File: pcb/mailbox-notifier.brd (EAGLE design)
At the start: 35 x 100 mm, 24 parts, among them Q1 AO3401, U1 MIC23155, U2 LTC2943-X, U3 FS312F-G, U4 FS8205, U5 MCP73832, U6 EFM32PG1B200_Q32, U7 RFM69HW

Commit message: PCB Work
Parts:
- removed U4: FS8205, Fortune:SOT23-6
- added C4: 100uF, Capacitor:CAP1206
- added C49: 100nF, Capacitor:CAP0603
- added CON1: 3P-SH-SIDE, JST:SH-03-SIDE
- added D2: SMAJ5.0A, TVS:DO214AC
- added F1: 1A Hold, PTC Fuses:1206
- added R1, R2: 5.1K Ohms, Resistor:RES0603
- added R58: 1K Ohms, Resistor:RES0603
- added R59: 100 Ohms, Resistor:RES0603
- added R63: 10M Ohm, Resistor:RES0603
- added U14: FS312F-G, Fortune:SOT23-6
- added U16: FS8205, Fortune:SOT23-6
- added U8: SI7021, Silicon Labs:DFN6
- U3: value FS312F-G -> 74LVC1G17; device Fortune:SOT23-6 -> Logic:SC70-5
- moved U6 81.8 mm to (18.0, 52.3)
- moved U3 79.6 mm to (-47.6, 32.8)
- moved TC1 14.7 mm to (3.50, 51.4)
- moved USB1 0.40 mm to (17.5, 98.6)
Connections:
- removed net +: BAT1.+
- removed net -: BAT1.-
- new net 5V0: C4.1, D1.A, D2.C, F1.1, Q1.1
- new net EXT_TRIG: U3.4
- new net GBAT: BAT1.-, C49.2, R63.2, U14.6, U16.3
- new net N$2: BAT1.+, U2.8
- new net N$3: R1.2, USB1.CC2
- new net N$4: F1.2, USB1.VBUS@0, USB1.VBUS@1
- new net N$47: U14.3, U16.6
- new net N$48: U14.1, U16.4
- new net N$49: R59.1, U14.5
- new net N$5: R2.2, USB1.CC1
- new net N$50: R58.1, U14.2
- new net N$6: CON1.2, U3.2
- new net VBAT: C49.1, Q1.3, R59.2, U2.1
- new net VIN: D1.C, Q1.2
- net 2V8: now also CON1.1, U3.5
- net GND: now also C4.2, CON1.3, D2.A, R1.1, R2.1, R58.2, R63.1, U16.1, U3.3, USB1.GND@0, USB1.GND@1, USB1.SHIELD@0, USB1.SHIELD@1, USB1.SHIELD@2, USB1.SHIELD@3

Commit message: PCB work
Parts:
- removed C49: 100nF, Capacitor:CAP0603
- removed R58: 1K Ohms, Resistor:RES0603
- removed R59: 100 Ohms, Resistor:RES0603
- removed R63: 10M Ohm, Resistor:RES0603
- removed U14: FS312F-G, Fortune:SOT23-6
- removed U16: FS8205, Fortune:SOT23-6
- removed U2: LTC2943-X, Analog Devices:DFN8
- removed U3: 74LVC1G17, Logic:SC70-5
- added C10: 2.2uF, Capacitor:CAP0603
- added C11: 100uF, Capacitor:CAP1206
- added C12, C14, C15, C20, C21, C23, C7: 100nF, Capacitor:CAP0603
- added C17, C24: 1uF, Capacitor:CAP0603
- added C22, C9: 470pF, Capacitor:CAP0603
- added C5, C6: 10uF, Capacitor:CAP0603
- added C8: 4.7uF, Capacitor:CAP0603
- added D3: SK9822, LED:2020
- added L2: 4.7uH, Inductor:IND0603
- added R10: 324K Ohms, Resistor:RES0603
- added R11: 91K Ohms, Resistor:RES0603
- added R12: 10M Ohm, Resistor:RES0603
- added R15: 10K Ohms, Resistor:RES0603
- added R16, R17, R18, R19, R20, R9: 100K Ohms, Resistor:RES0603
- added R21: 2K Ohms, Resistor:RES0603
- added R3: 5.1K Ohms, Resistor:RES0603
- added R7: 1K Ohms, Resistor:RES0603
- added R8: 100 Ohms, Resistor:RES0603
- added U10: SI7021, Silicon Labs:DFN6
- added U11: 74LVC1G17, Logic:SC70-5
- added U12: MIC2019, Microchip:SOT23-6
- added U4: MIC23155, Microchip:DFN10
- added U9: RFM69HW, HopeRF:RFM69W-XXXS2
- added X1: 40MHz, Crystal:4-SMD-3225
- C16: value 100nF -> 4.7uF
- C18: value 1uF -> 100nF
- C19: value 4.7uF -> 100nF
- C2: value 100nF -> 100uF; device Capacitor:CAP0603 -> Capacitor:CAP1206
- D1: value B0530W -> SMAJ5.0A; device Generic Diode:SOD-123 -> TVS:DO214AC
- D2: value SMAJ5.0A -> B0530W; device TVS:DO214AC -> Generic Diode:SOD-123
- L1: value 4.7uH -> 2.2uH; device Inductor:IND0603 -> Inductor:IND0805
- R13, R4: value 10K Ohms -> 100K Ohms
- R2: value 5.1K Ohms -> 2.2K Ohms
- U1: value MIC23155 -> MCP73832; device Microchip:DFN10 -> Microchip:SOT23-5
- U5: value MCP73832 -> FS312F-G; device Microchip:SOT23-5 -> Fortune:SOT23-6
- U6: value EFM32PG1B200_Q32 -> FS8205; device EFM32:QFN32 -> Fortune:SOT23-6
- U7: value RFM69HW -> EFM32PG1B200_Q32; device HopeRF:RFM69W-XXXS2 -> EFM32:QFN32
- U8: value SI7021 -> SST26VF016B; device Silicon Labs:DFN6 -> Microchip:WSOIC8
- moved RFCON1 105.3 mm to (3.00, 17.0)
- moved U5 93.9 mm to (28.9, 86.7)
- moved R14 90.1 mm to (28.2, 43.2), turned to 90 degrees
- moved S1 90.1 mm to (4.20, 39.6), turned to 90 degrees
- moved U8 84.8 mm to (17.7, 24.7), turned to 90 degrees
- moved CON1 81.6 mm to (33.0, 64.4), turned to 90 degrees
- moved U1 80.4 mm to (29.0, 83.2)
- moved F1 77.5 mm to (17.7, 88.5), turned to 90 degrees
- moved C4 76.9 mm to (29.2, 72.5)
- moved L1 72.3 mm to (-92.4, 76.1)
- moved R4 71.5 mm to (-77.3, 36.5)
- moved R1 68.9 mm to (10.0, 96.5)
- moved D2 67.7 mm to (-20.3, 120.7)
- moved C2 63.6 mm to (14.3, 88.5), turned to 90 degrees
- moved C18 60.9 mm to (-61.2, 54.8)
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- renumbered C1 to C13
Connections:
- removed net N$2: BAT1.+, U2.8
- new net !FLASH_CS: R16.1, U8.1
- new net 2V8_PGOOD: R9.1, U4.5
- new net BAT_STAT: R4.1, U1.1
- new net I2C0_SCL: R15.1, U10.6
- new net I2C0_SDA: R14.1, U10.1
- new net LED_EN: U12.3
- new net N$10: R2.2, U1.5
- new net N$11: R21.2, U12.5
- new net N$12: L1.1, U4.1
- new net N$13: R10.1, R11.2, U4.4
- new net N$14: C9.1, U4.6
- new net N$15: C24.1, D3.5, U12.6
- new net N$16: U7.6, X1.1
- new net N$17: U7.7, X1.3
- new net US1_CLK: D3.4
- new net US1_MOSI: D3.3
- new net VBAT_SENSE: C22.1, R19.1, R20.2
- new net VIN1: C3.1
- net !RFM_CS: now also R18.1, U7.13, U9.15; no longer R14.1, U6.13, U7.15
- net !RST: now also R13.1, U7.8; no longer R4.1, U6.8
- net 1V8: now also C16.1, L2.1, U7.28; no longer C19.1, L1.1, U6.28
- net 2V8: now also C10.1, C11.1, C14.1, C15.1, C18.1, C19.2, C20.1, C21.1, C23.1, L1.2, R10.2, R13.2, R15.2, R16.2, R18.2, R9.2, U10.5, U11.5, U12.1, U4.3, U7.22, U7.27, U7.30, U7.5, U8.3, U8.7, U8.8, U9.8; no longer C16.2, C2.1, C3.1, U3.5, U6.22, U6.27, U6.30, U6.5, U7.8
- net 5V0: now also C2.1, D1.C, D2.A, U1.4; no longer C4.1, D1.A, D2.C
- net EXT_TRIG: now also U11.4; no longer U3.4
- net GBAT: now also C12.2, R12.2, U5.6, U6.3; no longer C49.2, R63.2, U14.6, U16.3
- net GND: now also C10.2, C11.2, C14.2, C15.2, C16.2, C17.1, C18.2, C19.1, C20.2, C21.2, C22.2, C23.2, C24.2, C5.2, C6.2, C7.2, C8.2, C9.2, D1.A, D3.2, R11.1, R12.1, R17.1, R20.1, R21.1, R3.1, R7.1, U1.2, U10.2, U11.3, U12.2, U4.10, U4.11, U4.7, U6.1, U7.25, U7.33, U8.4, U9.11, U9.9, X1.2, X1.4; no longer C16.1, C18.1, C19.2, D2.A, R13.1, R58.2, R63.1, U16.1, U3.3, U6.25, U6.33, U7.11, U7.9
- net N$1: now also U9.10; no longer U7.10
- net N$19: now also L2.2, U7.26; no longer L1.2, U6.26
- net N$20: now also C17.2, U7.29; no longer C18.2, U6.29
- net N$47: now also U5.3, U6.6; no longer U14.3, U16.6
- net N$48: now also U5.1, U6.4; no longer U14.1, U16.4
- net N$49: now also R8.1, U5.5; no longer R59.1, U14.5
- net N$5: now also R3.2; no longer R2.2
- net N$50: now also R7.2, U5.2; no longer R58.1, U14.2
- net N$6: now also U11.2; no longer U3.2
- net RFM_IRQ: now also U7.31, U9.2; no longer U6.31, U7.2
- net RFM_RST: now also R17.2, U7.12, U9.1; no longer R13.2, U6.12, U7.1
- net SWCLK: now also U7.1; no longer U6.1
- net SWDIO: now also U7.2; no longer U6.2
- net SWO: now also U7.3; no longer U6.3
- net US0_CLK: now also U7.14, U8.6, U9.12; no longer U6.14, U7.12
- net US0_MISO: now also U7.16, U8.2, U9.13; no longer U6.16, U7.13
- net US0_MOSI: now also U7.15, U8.5, U9.14; no longer U6.15, U7.14
- net VBAT: now also BAT1.+, C12.1, C4.1, R19.2, R8.2, U1.3; no longer C49.1, R59.2, U2.1
- net VIN: now also C5.1, C6.1, C7.1, C8.1, D2.C, U4.2, U4.8, U4.9; no longer D1.C
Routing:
- net N$4: track 0.00 -> 9.10 mm
- net N$3: track 0.00 -> 7.66 mm
- net N$5: track 0.00 -> 7.16 mm
- net 5V0: track 0.00 -> 7.09 mm
- net N$1: track 0.00 -> 3.62 mm
- added copper zone on layer 1, net GND
- added copper zone on layer 16, net GND

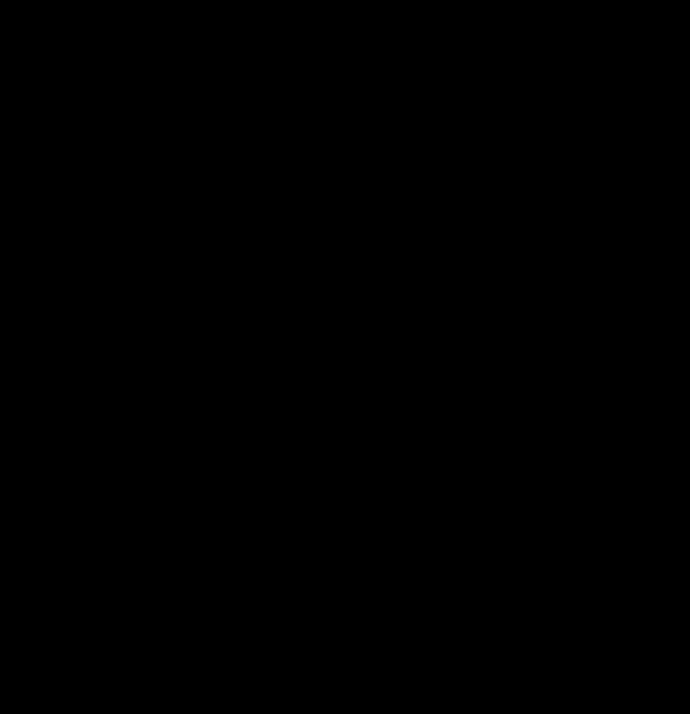
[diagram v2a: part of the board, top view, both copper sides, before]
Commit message: Add power switch to external trigger
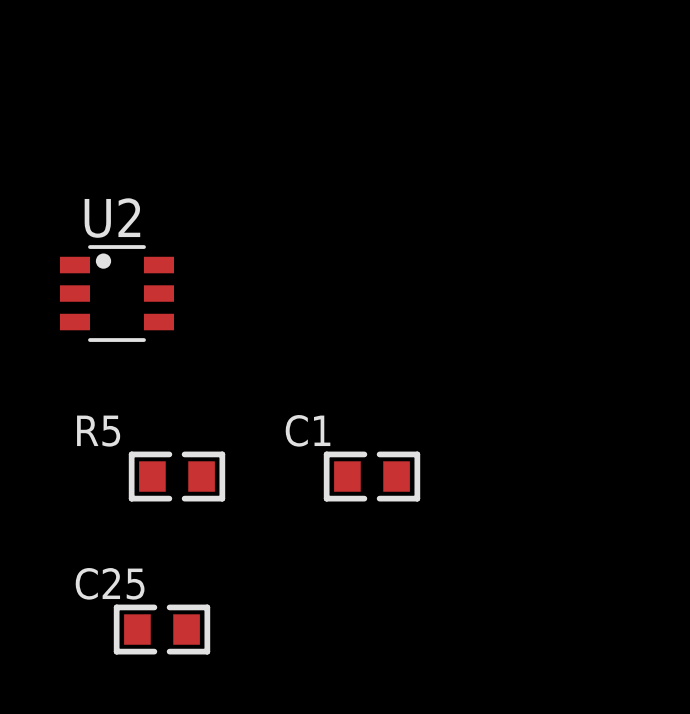
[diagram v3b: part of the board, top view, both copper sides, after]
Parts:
- added C1: 100nF, Capacitor:CAP0603
- added C25: 1uF, Capacitor:CAP0603
- added R5: 2K Ohms, Resistor:RES0603
- added U2: MIC2019, Microchip:SOT23-6
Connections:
- new net EXT_EN: U2.3
- new net N$2: R5.2, U2.5
- new net N$7: C25.1, CON1.1, U2.6
- net 2V8: now also C1.1, U2.1; no longer CON1.1
- net GND: now also C1.2, C25.2, R5.1, U2.2
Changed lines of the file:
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@@
 <?xml version="1.0" encoding="utf-8"?>
 <!DOCTYPE eagle SYSTEM "eagle.dtd">
-<eagle version="9.3.0">
+<eagle version="9.3.2">
 <drawing>
 <settings>
@@
 <attribute name="NAME" x="8.86" y="51.54" size="0.762" layer="25" font="vector" ratio="10"/>
 </element>
+<element name="U2" library="Microchip" package="SOT23-6" value="MIC2019" x="-94.5" y="-8.9" smashed="yes">
+<attribute name="NAME" x="-95.714" y="-7.0175" size="1.27" layer="25" ratio="10"/>
+<attribute name="VALUE" x="-95.714" y="-11.989" size="1.27" layer="27" ratio="10"/>
+</element>
+<element name="C1" library="Capacitor" package="CAP0603" value="100nF" x="-86" y="-15" smashed="yes">
+<attribute name="NAME" x="-88.9464" y="-13.984" size="1.016" layer="25" ratio="10" rot="SR0"/>
+<attribute name="VALUE" x="-88.9464" y="-17.032" size="1.016" layer="27" ratio="10" rot="SR0"/>
+</element>
+<element name="R5" library="Resistor" package="RES0603" value="2K Ohms" x="-92.5" y="-15" smashed="yes">
+<attribute name="NAME" x="-95.9544" y="-13.984" size="1.016" layer="25" ratio="10" rot="SR0"/>
+<attribute name="VALUE" x="-95.9544" y="-17.032" size="1.016" layer="27" ratio="10" rot="SR0"/>
+</element>
+<element name="C25" library="Capacitor" package="CAP0603" value="1uF" x="-93" y="-20.1" smashed="yes">
+<attribute name="NAME" x="-95.9464" y="-19.084" size="1.016" layer="25" ratio="10" rot="SR0"/>
+<attribute name="VALUE" x="-95.9464" y="-22.132" size="1.016" layer="27" ratio="10" rot="SR0"/>
+</element>
 </elements>
 <signals>
@@
 <contactref element="U9" pad="8"/>
 <contactref element="R18" pad="2"/>
-<contactref element="CON1" pad="1"/>
 <contactref element="U11" pad="5"/>
 <contactref element="R4" pad="2"/>
@@
 <contactref element="C23" pad="1"/>
 <contactref element="U12" pad="1"/>
-<wire x1="-38.91915" y1="115.6" x2="-24.58085" y2="115.6" width="0" layer="19" extent="1-1"/>
-<wire x1="-44.01915" y1="115.6" x2="-38.91915" y2="115.6" width="0" layer="19" extent="1-1"/>
-<wire x1="-49.11915" y1="115.6" x2="-44.01915" y2="115.6" width="0" layer="19" extent="1-1"/>
-<wire x1="-52.48085" y1="115.6" x2="-49.11915" y2="115.6" width="0" layer="19" extent="1-1"/>
-<wire x1="-62.68085" y1="106.7" x2="-52.48085" y2="115.6" width="0" layer="19" extent="1-1"/>
-<wire x1="-91.4348" y1="76.1" x2="-62.68085" y2="106.7" width="0" layer="19" extent="1-1"/>
-<wire x1="-93.7494" y1="68.6" x2="-91.4348" y2="76.1" width="0" layer="19" extent="1-1"/>
-<wire x1="-93.71915" y1="61.4" x2="-93.7494" y2="68.6" width="0" layer="19" extent="1-1"/>
-<wire x1="-91.58085" y1="56.3" x2="-93.71915" y2="61.4" width="0" layer="19" extent="1-1"/>
-<wire x1="-91.58085" y1="35.9" x2="-91.58085" y2="56.3" width="0" layer="19" extent="1-1"/>
-<wire x1="-78.61915" y1="33" x2="-91.58085" y2="35.9" width="0" layer="19" extent="1-1"/>
+<contactref element="C1" pad="1"/>
+<contactref element="U2" pad="1"/>
+<wire x1="-86.81915" y1="-15" x2="-95.9" y2="-7.95" width="0" layer="19" extent="1-1"/>
+<wire x1="-62.01915" y1="7.6" x2="-86.81915" y2="-15" width="0" layer="19" extent="1-1"/>
+<wire x1="-78.61915" y1="27.9" x2="-62.01915" y2="7.6" width="0" layer="19" extent="1-1"/>
+<wire x1="-78.61915" y1="33" x2="-78.61915" y2="27.9" width="0" layer="19" extent="1-1"/>
 <wire x1="-76.48085" y1="36.5" x2="-78.61915" y2="33" width="0" layer="19" extent="1-1"/>
-<wire x1="-78.61915" y1="27.9" x2="-78.61915" y2="33" width="0" layer="19" extent="1-1"/>
+<wire x1="-91.58085" y1="35.9" x2="-78.61915" y2="33" width="0" layer="19" extent="1-1"/>
+<wire x1="-91.58085" y1="56.3" x2="-91.58085" y2="35.9" width="0" layer="19" extent="1-1"/>
+<wire x1="-93.71915" y1="61.4" x2="-91.58085" y2="56.3" width="0" layer="19" extent="1-1"/>
+<wire x1="-93.7494" y1="68.6" x2="-93.71915" y2="61.4" width="0" layer="19" extent="1-1"/>
+<wire x1="-91.4348" y1="76.1" x2="-93.7494" y2="68.6" width="0" layer="19" extent="1-1"/>
 <wire x1="-59.88085" y1="49.7" x2="-76.48085" y2="36.5" width="0" layer="19" extent="1-1"/>
 <wire x1="-62.01915" y1="54.8" x2="-59.88085" y2="49.7" width="0" layer="19" extent="1-1"/>
-<wire x1="-62.01915" y1="7.6" x2="-78.61915" y2="27.9" width="0" layer="19" extent="1-1"/>
+<wire x1="-62.68085" y1="106.7" x2="-91.4348" y2="76.1" width="0" layer="19" extent="1-1"/>
+<wire x1="-52.48085" y1="115.6" x2="-62.68085" y2="106.7" width="0" layer="19" extent="1-1"/>
+<wire x1="-49.11915" y1="115.6" x2="-52.48085" y2="115.6" width="0" layer="19" extent="1-1"/>
+<wire x1="-44.01915" y1="115.6" x2="-49.11915" y2="115.6" width="0" layer="19" extent="1-1"/>
+<wire x1="-38.91915" y1="115.6" x2="-44.01915" y2="115.6" width="0" layer="19" extent="1-1"/>
+<wire x1="-24.58085" y1="115.6" x2="-38.91915" y2="115.6" width="0" layer="19" extent="1-1"/>
 <wire x1="4.135" y1="48.86" x2="-59.88085" y2="49.7" width="0" layer="19" extent="1-1"/>
 <wire x1="15.57" y1="52.05" x2="4.135" y2="48.86" width="0" layer="19" extent="1-1"/>
@@
 <wire x1="16.95" y1="63.7" x2="17.25" y2="54.73" width="0" layer="19" extent="1-1"/>
 <wire x1="24.4" y1="63.75" x2="16.95" y2="63.7" width="0" layer="19" extent="1-1"/>
-<wire x1="30.025" y1="63.4" x2="24.4" y2="63.75" width="0" layer="19" extent="1-1"/>
-<wire x1="29.8" y1="55.9" x2="30.025" y2="63.4" width="0" layer="19" extent="1-1"/>
+<wire x1="29.8" y1="55.9" x2="24.4" y2="63.75" width="0" layer="19" extent="1-1"/>
 <wire x1="30" y1="44.01915" x2="29.8" y2="55.9" width="0" layer="19" extent="1-1"/>
 <wire x1="28.2" y1="44.01915" x2="30" y2="44.01915" width="0" layer="19" extent="1-1"/>
@@
 <vertex x="-3.2" y="-3.7"/>
 </polygon>
+<contactref element="C1" pad="2"/>
+<contactref element="U2" pad="2"/>
+<contactref element="R5" pad="1"/>
+<contactref element="C25" pad="2"/>
 <wire x1="21.82" y1="98.6" x2="25.81915" y2="96.5" width="0" layer="19" extent="1-1"/>
 <wire x1="21.82" y1="94.42" x2="21.82" y2="98.6" width="0" layer="19" extent="1-1"/>
@@
 <wire x1="-60.38085" y1="-2.6" x2="-61.51915" y2="2.5" width="0" layer="19" extent="1-1"/>
 <wire x1="-60.38085" y1="54.8" x2="-61.51915" y2="29.3" width="0" layer="19" extent="1-1"/>
+<wire x1="-85.18085" y1="-15" x2="-60.38085" y2="-2.6" width="0" layer="19" extent="1-1"/>
+<wire x1="-93.31915" y1="-15" x2="-85.18085" y2="-15" width="0" layer="19" extent="1-1"/>
+<wire x1="-92.18085" y1="-20.1" x2="-93.31915" y2="-15" width="0" layer="19" extent="1-1"/>
+<wire x1="-95.9" y1="-8.9" x2="-93.31915" y2="-15" width="0" layer="19" extent="1-1"/>
 </signal>
 <signal name="SWO">
@@
 <wire x1="15.57" y1="51.05" x2="12.5" y2="48.2" width="0" layer="19" extent="1-1"/>
 </signal>
+<signal name="N$2">
+<contactref element="R5" pad="2"/>
+<contactref element="U2" pad="5"/>
+<wire x1="-93.1" y1="-8.9" x2="-91.68085" y2="-15" width="0" layer="19" extent="1-1"/>
+</signal>
+<signal name="N$7">
+<contactref element="U2" pad="6"/>
+<contactref element="C25" pad="1"/>
+<contactref element="CON1" pad="1"/>
+<wire x1="-93.1" y1="-7.95" x2="-93.81915" y2="-20.1" width="0" layer="19" extent="1-1"/>
+<wire x1="30.025" y1="63.4" x2="-93.1" y2="-7.95" width="0" layer="19" extent="1-1"/>
+</signal>
+<signal name="EXT_EN">
+<contactref element="U2" pad="3"/>
+</signal>
 </signals>

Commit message: PCB work
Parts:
- removed C24, C25: 1uF, Capacitor:CAP0603
- removed R21: 2K Ohms, Resistor:RES0603
- removed U12: MIC2019, Microchip:SOT23-6
- added R6: 100K Ohms, Resistor:RES0603
- added U3: FS312F-G, Fortune:SOT23-6
- C10: value 2.2uF -> 100uF; device Capacitor:CAP0603 -> Capacitor:CAP1206
- C11: value 100uF -> 100nF; device Capacitor:CAP1206 -> Capacitor:CAP0603
- C15: value 100nF -> 4.7uF
- C16: value 4.7uF -> 1uF
- C17: value 1uF -> 100nF
- C22: value 470pF -> 1uF
- C23: value 100nF -> 1uF
- C3: value 100nF -> 100uF; device Capacitor:CAP0603 -> Capacitor:CAP1206
- C4: value 100uF -> 10uF; device Capacitor:CAP1206 -> Capacitor:CAP0603
- C6: value 10uF -> 470pF
- C8: value 4.7uF -> 470pF
- C9: value 470pF -> 2.2uF
- R19, R20: value 100K Ohms -> 2K Ohms
- R5: value 2K Ohms -> 100K Ohms
- U10: value SI7021 -> MIC2019; device Silicon Labs:DFN6 -> Microchip:SOT23-6
- U2: value MIC2019 -> MIC23155; device Microchip:SOT23-6 -> Microchip:DFN10
- U4: value MIC23155 -> FS8205; device Microchip:DFN10 -> Fortune:SOT23-6
- U5: value FS312F-G -> EFM32PG1B200F256GM32; device Fortune:SOT23-6 -> EFM32:QFN32
- U6: value FS8205 -> SST26VF016B; device Fortune:SOT23-6 -> Microchip:WSOIC8
- U7: value EFM32PG1B200_Q32 -> RFM69HW; device EFM32:QFN32 -> HopeRF:RFM69W-XXXS2
- U8: value SST26VF016B -> SI7021; device Microchip:WSOIC8 -> Silicon Labs:DFN6
- U9: value RFM69HW -> MIC2019; device HopeRF:RFM69W-XXXS2 -> Microchip:SOT23-6
- moved R5 160.3 mm to (29.1, 89.5)
- moved C1 145.1 mm to (22.3, 81.5), turned to 270 degrees
- moved U2 138.6 mm to (16.1, 74.7), turned to 90 degrees
- moved R2 124.8 mm to (29.1, 83.0), turned to 180 degrees
- moved R9 122.6 mm to (24.8, 71.9), turned to 270 degrees
- moved C8 118.3 mm to (20.3, 75.4), turned to 90 degrees
- moved C3 117.6 mm to (24.6, 81.5), turned to 270 degrees
- moved R11 116.5 mm to (22.2, 71.9), turned to 90 degrees
- moved C19 114.4 mm to (31.8, 39.2), turned to 90 degrees
- moved R10 113.8 mm to (20.3, 71.9), turned to 270 degrees
- moved C17 111.9 mm to (10.0, 27.1), turned to 90 degrees
- moved C20 110.6 mm to (30.6, 54.9), turned to 180 degrees
- moved C9 110.5 mm to (16.0, 64.8), turned to 180 degrees
- moved R4 109.9 mm to (26.7, 71.9), turned to 270 degrees
- moved C6 109.2 mm to (11.5, 59.3), turned to 90 degrees
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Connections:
- removed net VIN1: C3.1
- net !FLASH_CS: now also U5.16, U6.1; no longer U8.1
- net !RFM_CS: now also U5.14, U7.15; no longer U7.13, U9.15
- net !RST: now also U5.8; no longer U7.8
- net 1V8: now also C15.1, U5.28; no longer C16.1, U7.28
- net 2V8: now also C12.1, C17.1, C18.2, C19.1, C9.1, U10.1, U2.3, U5.22, U5.27, U5.30, U5.5, U6.3, U6.7, U6.8, U7.8, U8.5, U9.1; no longer C1.1, C11.1, C15.1, C18.1, C19.2, C23.1, U10.5, U12.1, U2.1, U4.3, U7.22, U7.27, U7.30, U7.5, U8.3, U8.7, U8.8, U9.8
- net 2V8_PGOOD: now also U2.5, U5.4; no longer U4.5
- net BAT_STAT: now also U5.31
- net EXT_EN: now also U10.3, U5.23; no longer U2.3
- net EXT_TRIG: now also U5.24
- net GBAT: now also C11.2, U3.6, U4.3; no longer C12.2, U5.6, U6.3
- net GND: now also C12.2, C16.1, C17.2, C18.1, C19.2, R19.1, R6.1, U2.10, U2.11, U2.7, U4.1, U5.25, U5.33, U6.4, U7.11, U7.9, U8.2, U9.2; no longer C11.2, C16.2, C17.1, C18.2, C19.1, C24.2, C25.2, R21.1, R5.1, U12.2, U2.2, U4.10, U4.11, U4.7, U6.1, U7.25, U7.33, U8.4, U9.11, U9.9
- net I2C0_SCL: now also U5.21, U8.6; no longer U10.6
- net I2C0_SDA: now also U5.20, U8.1; no longer U10.1
- net LED_EN: now also U5.19, U9.3; no longer U12.3
- net N$1: now also U7.10; no longer U9.10
- net N$11: now also R19.2, U9.5; no longer R21.2, U12.5
- net N$12: now also U2.1; no longer U4.1
- net N$13: now also U2.4; no longer U4.4
- net N$14: now also C8.1, U2.6; no longer C9.1, U4.6
- net N$15: now also C22.1, U9.6; no longer C24.1, U12.6
- net N$16: now also U5.6; no longer U7.6
- net N$17: now also U5.7; no longer U7.7
- net N$19: now also U5.26; no longer U7.26
- net N$2: now also R20.2, U10.5; no longer R5.2, U2.5
- net N$20: now also C16.2, U5.29; no longer C17.2, U7.29
- net N$47: now also U3.3, U4.6; no longer U5.3, U6.6
- net N$48: now also U3.1, U4.4; no longer U5.1, U6.4
- net N$49: now also U3.5; no longer U5.5
- net N$50: now also U3.2; no longer U5.2
- net N$7: now also C23.1, U10.6; no longer C25.1, U2.6
- net RFM_IRQ: now also U5.15, U7.2; no longer U7.31, U9.2
- net RFM_RST: now also U5.13, U7.1; no longer U7.12, U9.1
- net SWCLK: now also U5.1; no longer U7.1
- net SWDIO: now also U5.2; no longer U7.2
- net SWO: now also U5.3; no longer U7.3
- net US0_CLK: now also U5.10, U6.6, U7.12; no longer U7.14, U8.6, U9.12
- net US0_MISO: now also U5.12, U6.2, U7.13; no longer U7.16, U8.2, U9.13
- net US0_MOSI: now also U5.11, U6.5, U7.14; no longer U7.15, U8.5, U9.14
- net US1_CLK: now also U5.18
- net US1_MOSI: now also U5.17
- net VBAT: now also C1.1, C11.1, C3.1, R5.2; no longer C12.1, C4.1, R19.2
- net VBAT_SENSE: now also C6.1, R5.1, R6.2, U5.32; no longer C22.1, R19.1, R20.2
- net VIN: now also C4.1, U2.2, U2.8, U2.9; no longer C6.1, C8.1, U4.2, U4.8, U4.9
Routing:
- net 2V8: track 0.00 -> 212.0 mm, vias 0 -> 14
- net GBAT: track 0.00 -> 96.2 mm, vias 0 -> 2
- net VBAT: track 0.00 -> 40.9 mm, vias 0 -> 3
- net !RST: track 0.00 -> 35.5 mm, vias 0 -> 2
- net VIN: track 0.00 -> 22.7 mm, vias 0 -> 2
- net US1_MOSI: track 0.00 -> 22.2 mm, vias 0 -> 2
- net US1_CLK: track 0.00 -> 19.2 mm, vias 0 -> 2
- net I2C0_SCL: track 0.00 -> 18.5 mm, vias 0 -> 3
- net LED_EN: track 0.00 -> 17.4 mm, vias 0 -> 2
- net SWO: track 0.00 -> 17.3 mm, vias 0 -> 2
- net 5V0: track 7.09 -> 22.9 mm
- net I2C0_SDA: track 0.00 -> 15.1 mm, vias 0 -> 2
- net SWDIO: track 0.00 -> 13.1 mm
- net SWCLK: track 0.00 -> 11.5 mm
- net N$15: track 0.00 -> 9.48 mm
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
